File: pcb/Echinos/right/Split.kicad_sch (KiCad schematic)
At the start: 44 parts, among them J200 USB_B_Micro, J201 Conn_01x04_Socket, J202 Conn_01x12_Socket, J203 Conn_01x06_Socket, J204 Conn_01x06_Socket, J205 Conn_01x06_Socket, J206 USB_C_Receptacle_USB2.0, J207 Conn_01x05_Socket, U202 USBLC6-2P6, U203 74LVC1T45, U204 USBLC6-2P6, U205 XC6210B332MR-G

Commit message: 💥 [PCB] - Group left and right on the same PCB.   - Schematics are different for each side   - Split trace naming to avoid mixing right and left   - Add mouse bite between both halves to make manufacturing easier (new footprint)
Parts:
- removed A1: Echinos Logo, Echinos:Graphics_Hedgehog, symbol Mechanical:Fiducial
- added A200: Echinos Logo, Echinos:Graphics_Hedgehog, symbol Mechanical:Fiducial
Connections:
- net +3.3V renamed +3V3_R
- net +5V renamed +5V_R
- net GND renamed GND_R
- net P_RX renamed RX_split_R
- net P_TX renamed TX_split_R
- net VBUS_split renamed VBUS_split_R
- net col1 renamed col1_R
- net col2 renamed col2_R
- net col3 renamed col3_R
- net col4 renamed col4_R
- net col5 renamed col5_R
- net col6 renamed col6_R
- net row6 renamed row6_R
- net row7 renamed row7_R
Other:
- sheet Backlight ports: added +5V; removed none
- sheet RP2040 ports: added +1V1; removed none

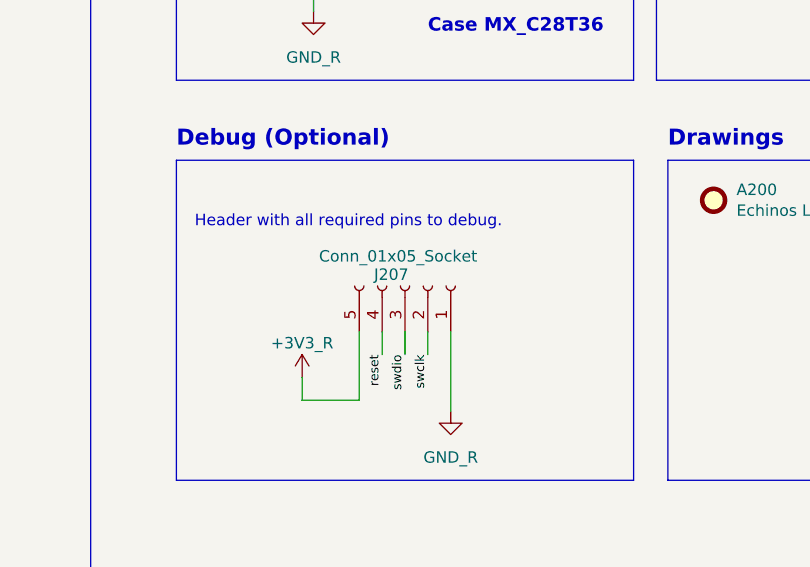
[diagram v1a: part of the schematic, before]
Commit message: 💄 [PCB] - Please DRC at RP2040 level with at least 2 connections on each via for thermal relief. Flip Debug connector to avoid match convention used for pin 1 (squared one) the same as for split connector breakout connectors (power on both).
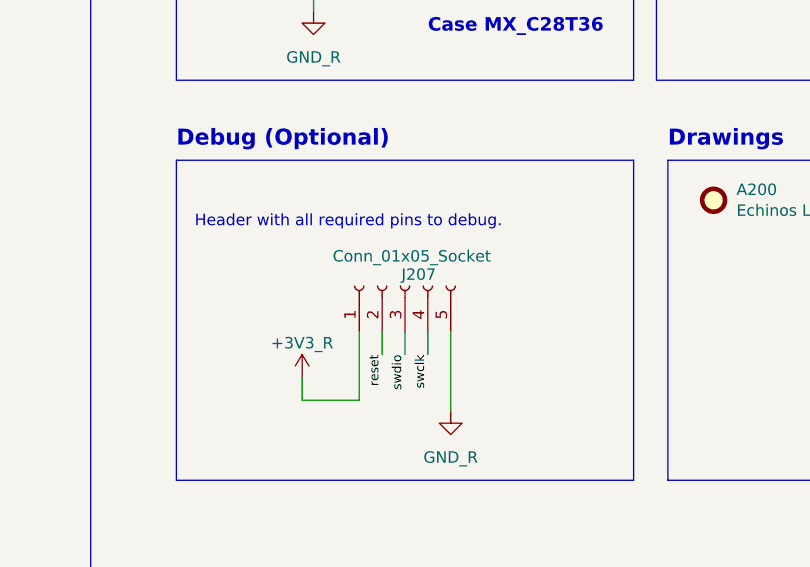
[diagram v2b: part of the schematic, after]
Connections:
- net +3V3_R: now also J207.1 (Pin_1); no longer J207.5 (Pin_5)
- net GND_R: now also J207.5 (Pin_5); no longer J207.1 (Pin_1)
- net reset: now also J207.2 (Pin_2); no longer J207.4 (Pin_4)
- net swclk: now also J207.4 (Pin_4); no longer J207.2 (Pin_2)
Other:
- moved on the sheet: J207
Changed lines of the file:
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@@
 	(symbol
 		(lib_id "Connector:Conn_01x05_Socket")
-		(at 325.12 222.25 270)
-		(mirror x)
+		(at 325.12 222.25 90)
 		(unit 1)
 		(body_style 1)
@@
 		(dnp no)
 		(property "Reference" "J207"
-			(at 323.596 220.98 90)
+			(at 326.644 220.98 90)
 			(show_name no)
 			(do_not_autoplace no)
@@
 		)
 		(property "Value" "Conn_01x05_Socket"
-			(at 324.358 218.948 90)
+			(at 325.882 218.948 90)
 			(show_name no)
 			(do_not_autoplace no)
